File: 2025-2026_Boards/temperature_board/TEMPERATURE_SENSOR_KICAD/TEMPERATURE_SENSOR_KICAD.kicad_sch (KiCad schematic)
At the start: 79 parts, among them J1 LCD Connector Pinout, Q1 Q_NPN_BCE, Q3 Q_NPN_BCE, Q4 Q_NPN_BCE, Q5 Q_PNP_BCE, U1 STM32G431CBT6, U2 TMP235A4DBZR, U3 AMS1117-3.3, U5 TPS62932DRLR, U8 AMS1117

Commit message: redid led display. can i delete the 2.2v regulator?
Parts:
- R11, R8: footprint Resistor_SMD:R_0402_1005Metric -> Resistor_SMD:R_0201_0603Metric
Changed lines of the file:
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@@
 			)
 		)
-		(property "Footprint" "Resistor_SMD:R_0402_1005Metric"
+		(property "Footprint" "Resistor_SMD:R_0201_0603Metric"
 			(at 22.86 123.952 90)
 			(effects
@@
 			)
 		)
-		(property "Footprint" "Resistor_SMD:R_0402_1005Metric"
+		(property "Footprint" "Resistor_SMD:R_0201_0603Metric"
 			(at 30.48 129.032 90)
 			(effects

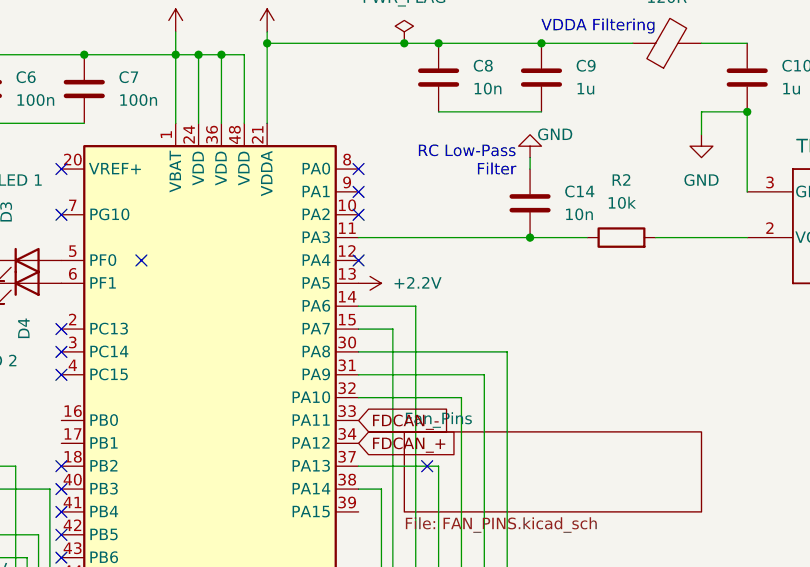
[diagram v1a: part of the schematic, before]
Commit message: redid led display.
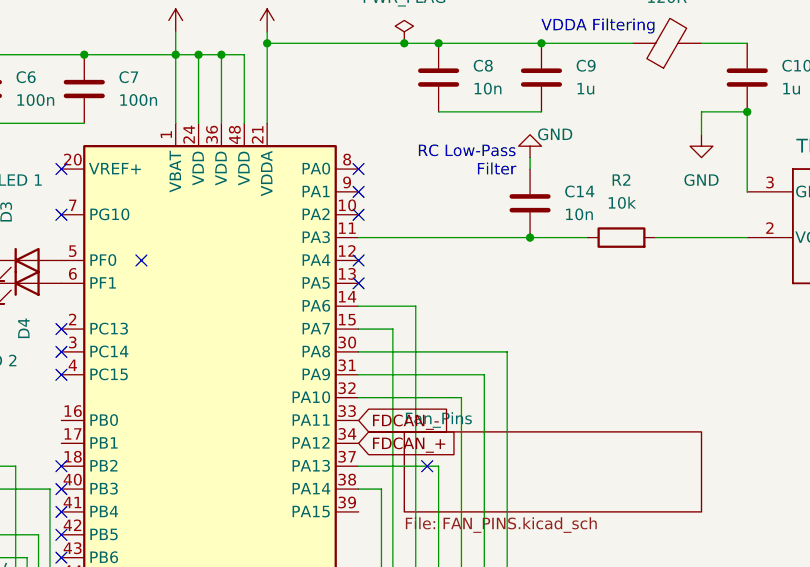
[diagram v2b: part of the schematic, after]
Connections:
- net +2.2V: no longer U1.13 (PA5)
- no-connect marks 23 -> 24
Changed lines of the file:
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@@
 	)
 	(no_connect
+		(at 93.98 95.25)
+	)
+	(no_connect
 		(at 60.96 100.33)
 	)
@@
 					(unit 1)
 				)
-			)
-		)
-	)
-	(symbol
-		(lib_id "power:+3.3V")
-		(at 93.98 95.25 270)
-		(unit 1)
-		(exclude_from_sim no)
-		(in_bom yes)
-		(on_board yes)
-		(dnp no)
-		(fields_autoplaced yes)
-		(property "Reference" "#PWR067"
-			(at 90.17 95.25 0)
-			(effects
-				(font
-					(size 1.27 1.27)
-				)
-				(hide yes)
-			)
-		)
-		(property "Value" "+2.2V"
-			(at 97.79 95.2499 90)
-			(effects
-				(font
-					(size 1.27 1.27)
-				)
-				(justify left)
-			)
-		)
-		(property "Footprint" ""
-			(at 93.98 95.25 0)
-			(effects
-				(font
-					(size 1.27 1.27)
-				)
-				(hide yes)
-			)
-		)
-		(property "Datasheet" ""
-			(at 93.98 95.25 0)
-			(effects
-				(font
-					(size 1.27 1.27)
-				)
-				(hide yes)
-			)
-		)
-		(property "Description" "Power symbol creates a global label with name \"+3.3V\""
-			(at 93.98 95.25 0)
-			(effects
-				(font
-					(size 1.27 1.27)
-				)
-				(hide yes)
-			)
-		)
-		(pin "1"
-		)
-		(instances
-			(project ""
-				(path "/0800d6d6-19ae-426e-ad65-5e021a8f0397"
-					(reference "#PWR067")
-					(unit 1)
-				)

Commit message: rehashed
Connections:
- no-connect marks 24 -> 26
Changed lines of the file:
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@@
 	)
 	(no_connect
-		(at 101.6 115.57)
+		(at 93.98 120.65)
+	)
+	(no_connect
+		(at 60.96 113.03)
 	)
 	(no_connect
@@
 	)
 	(no_connect
+		(at 60.96 110.49)
+	)
+	(no_connect

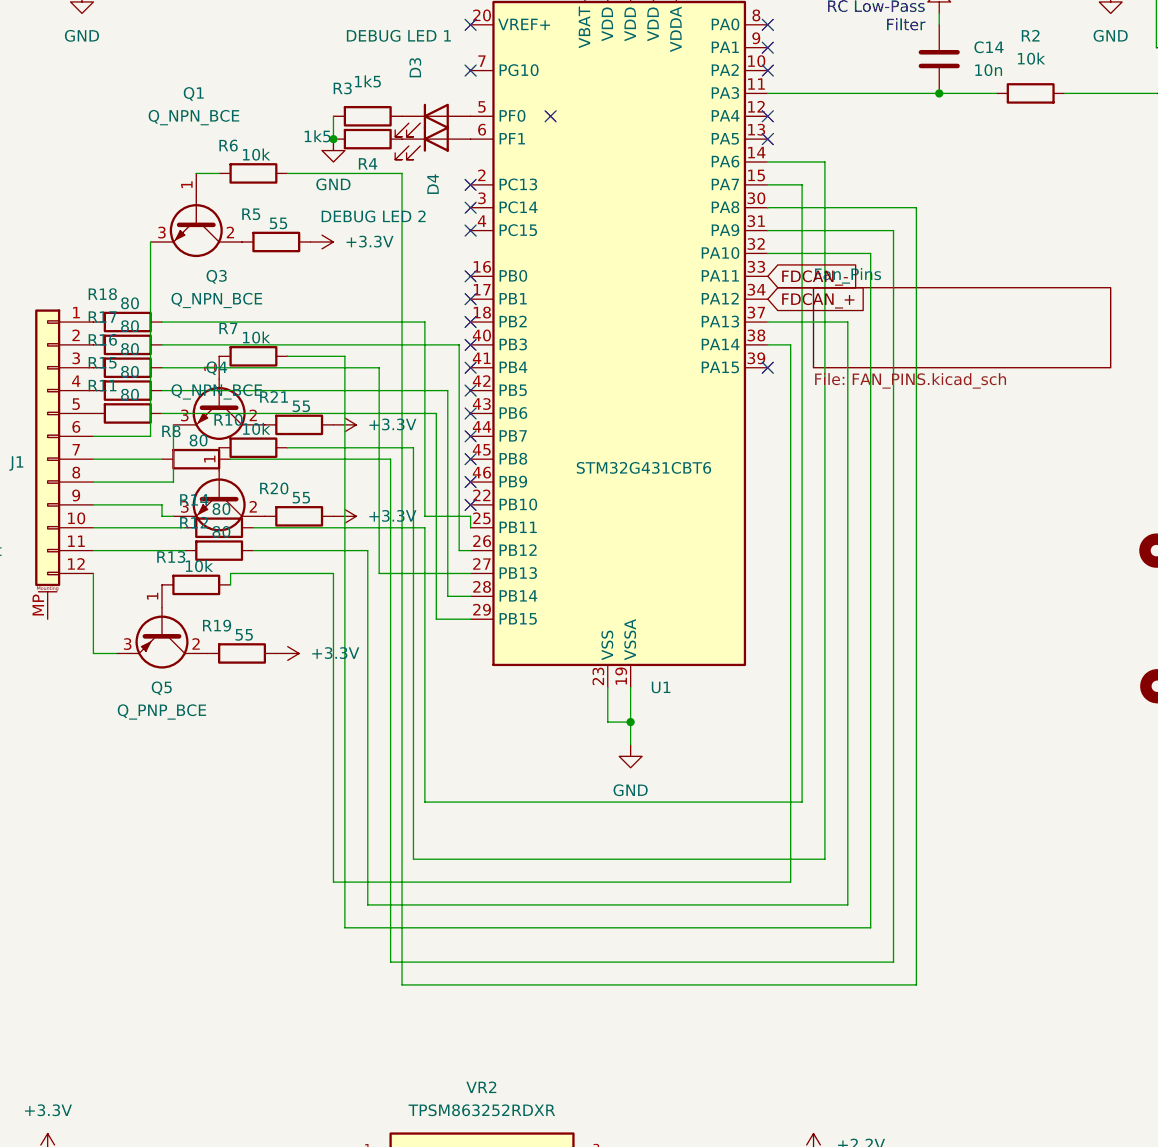
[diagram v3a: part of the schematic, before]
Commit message: reduced #vias
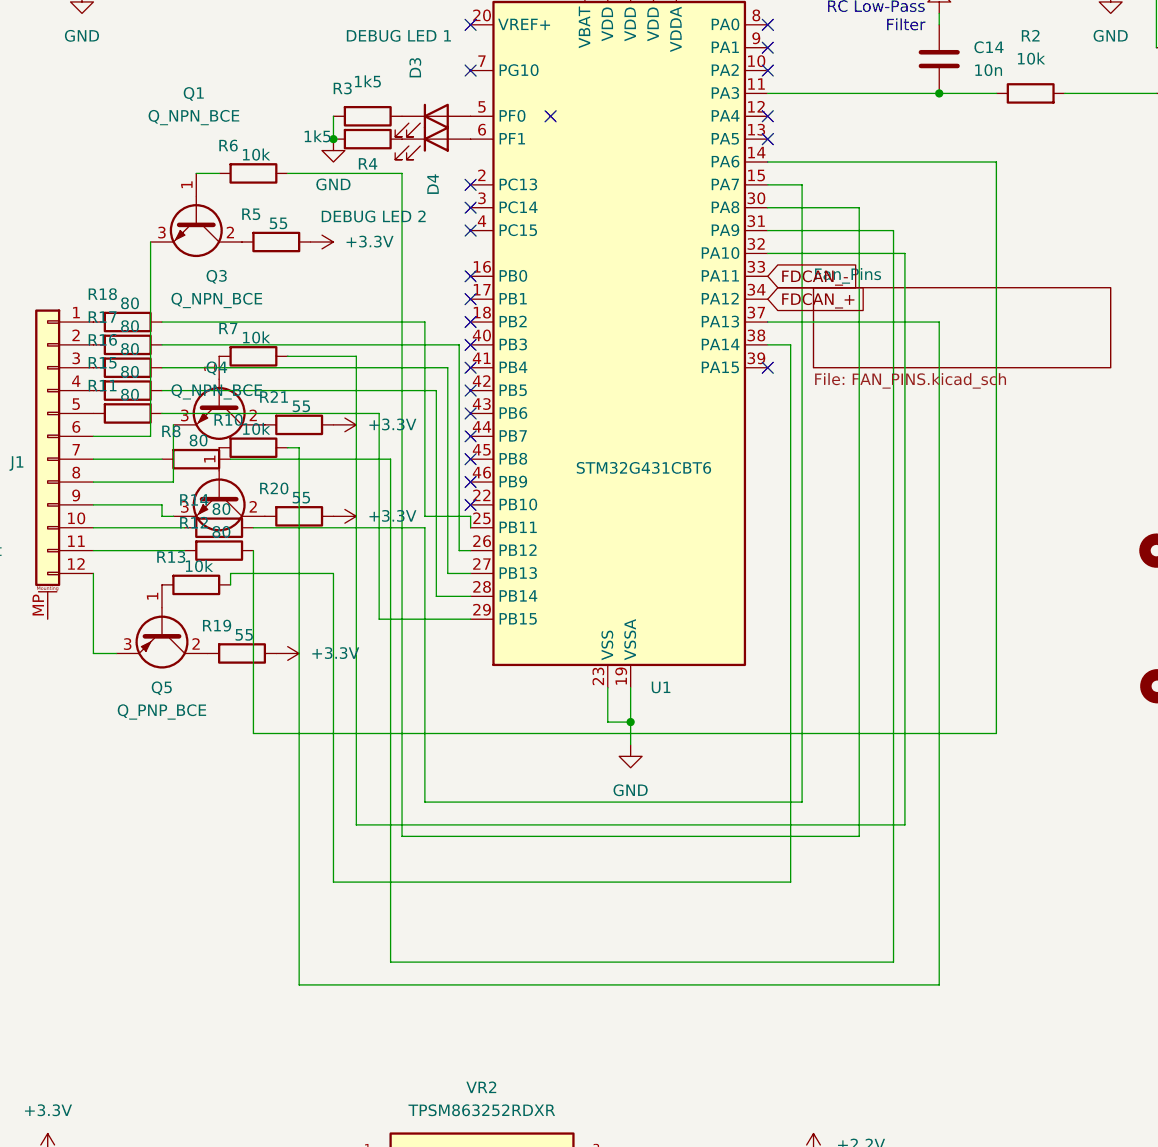
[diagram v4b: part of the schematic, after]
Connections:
- net at R12.1: now also U1.14 (PA6); no longer U1.37 (PA13)
- net at R10.1: now also U1.37 (PA13); no longer U1.14 (PA6)
